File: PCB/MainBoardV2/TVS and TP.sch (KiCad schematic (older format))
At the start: 15 parts, among them U10 AOZ8318DI, U11 AOZ8318DI, U12 AOZ8318DI

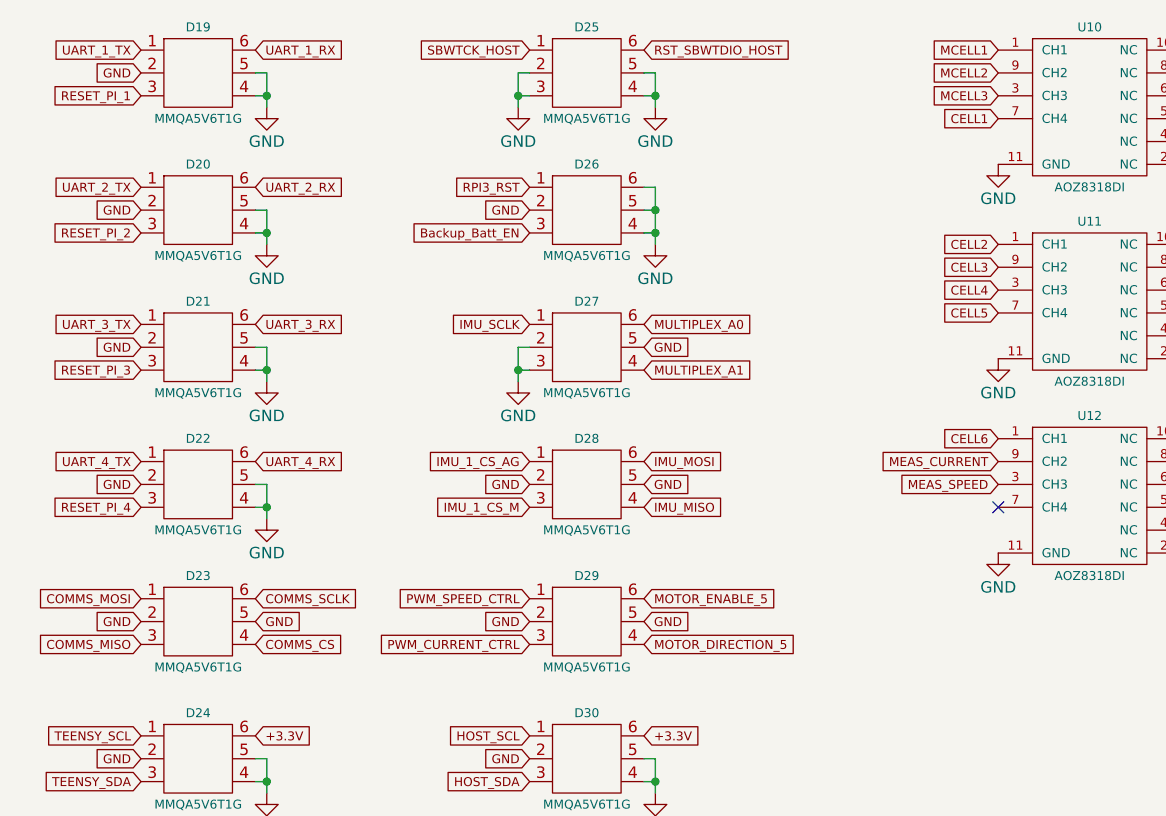
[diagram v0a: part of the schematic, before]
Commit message: Layout Done - Needs TPs Still
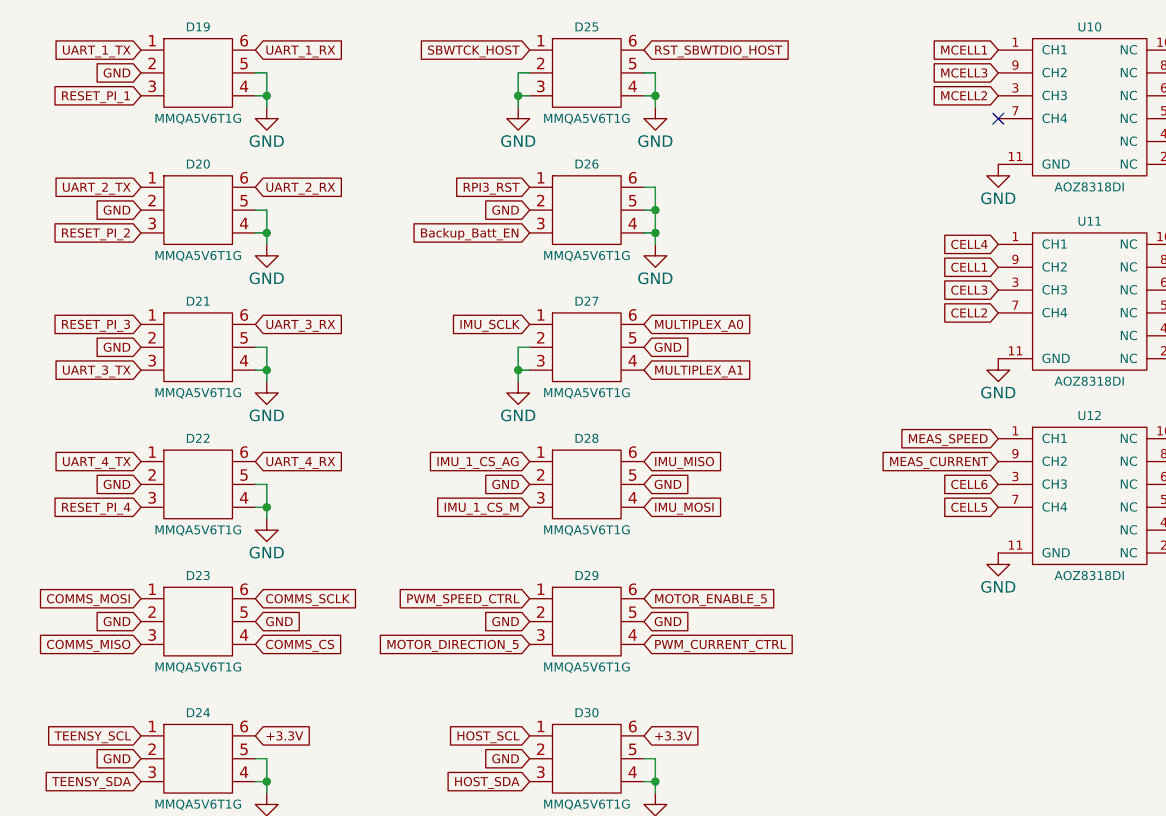
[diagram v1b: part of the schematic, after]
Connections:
- net CELL1: now also U11.9 (CH2); no longer U10.7 (CH4)
- net CELL2: now also U11.7 (CH4); no longer U11.1 (CH1)
- net CELL3: now also U11.3 (CH3); no longer U11.9 (CH2)
- net CELL4: now also U11.1 (CH1); no longer U11.3 (CH3)
- net CELL5: now also U12.7 (CH4); no longer U11.7 (CH4)
- net CELL6: now also U12.3 (CH3); no longer U12.1 (CH1)
- net IMU_MISO: now also D28.6; no longer D28.4
- net IMU_MOSI: now also D28.4; no longer D28.6
- net MCELL2: now also U10.3 (CH3); no longer U10.9 (CH2)
- net MCELL3: now also U10.9 (CH2); no longer U10.3 (CH3)
- net MEAS_SPEED: now also U12.1 (CH1); no longer U12.3 (CH3)
- net MOTOR_DIRECTION_5: now also D29.3; no longer D29.4
- net PWM_CURRENT_CTRL: now also D29.4; no longer D29.3
- net RESET_PI_3: now also D21.1; no longer D21.3
- net UART_3_TX: now also D21.3; no longer D21.1
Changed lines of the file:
@@
 RESET_PI_1
 $Comp
-L GND #PWR60
+L GND #PWR061
 U 1 1 5A7224CC
 P 1650 1350
-F 0 "#PWR60" H 1650 1100 50  0001 C CNN
+F 0 "#PWR061" H 1650 1100 50  0001 C CNN
 F 1 "GND" H 1650 1200 50  0000 C CNN
 F 2 "" H 1650 1350 50  0000 C CNN
@@
 RESET_PI_2
 $Comp
-L GND #PWR61
+L GND #PWR062
 U 1 1 5A722ECA
 P 1650 1950
-F 0 "#PWR61" H 1650 1700 50  0001 C CNN
+F 0 "#PWR062" H 1650 1700 50  0001 C CNN
 F 1 "GND" H 1650 1800 50  0000 C CNN
 F 2 "" H 1650 1950 50  0000 C CNN
@@
 	1    0    0    -1
 $EndComp
-Text GLabel 1100 2300 0    39   Input ~ 0
+Text GLabel 1100 2500 0    39   Input ~ 0
 UART_3_TX
 Text GLabel 1600 2300 2    39   Input ~ 0
 UART_3_RX
-Text GLabel 1100 2500 0    39   Input ~ 0
+Text GLabel 1100 2300 0    39   Input ~ 0
 RESET_PI_3
 $Comp
-L GND #PWR62
+L GND #PWR063
 U 1 1 5A722F46
 P 1650 2550
-F 0 "#PWR62" H 1650 2300 50  0001 C CNN
+F 0 "#PWR063" H 1650 2300 50  0001 C CNN
 F 1 "GND" H 1650 2400 50  0000 C CNN
 F 2 "" H 1650 2550 50  0000 C CNN
@@
 RESET_PI_4
 $Comp
-L GND #PWR63
+L GND #PWR064
 U 1 1 5A722F5A
 P 1650 3150
-F 0 "#PWR63" H 1650 2900 50  0001 C CNN
+F 0 "#PWR064" H 1650 2900 50  0001 C CNN
 F 1 "GND" H 1650 3000 50  0000 C CNN
 F 2 "" H 1650 3150 50  0000 C CNN
@@
 GND
 $Comp
-L GND #PWR64
+L GND #PWR065
 U 1 1 5A725481
 P 1650 4350
-F 0 "#PWR64" H 1650 4100 50  0001 C CNN
+F 0 "#PWR065" H 1650 4100 50  0001 C CNN
 F 1 "GND" H 1650 4200 50  0000 C CNN
 F 2 "" H 1650 4350 50  0000 C CNN
@@
 GND
 $Comp
-L GND #PWR69
+L GND #PWR066
 U 1 1 5A726700
 P 3350 4350
-F 0 "#PWR69" H 3350 4100 50  0001 C CNN
+F 0 "#PWR066" H 3350 4100 50  0001 C CNN
 F 1 "GND" H 3350 4200 50  0000 C CNN
 F 2 "" H 3350 4350 50  0000 C CNN
@@
 Text GLabel 3300 3500 2    39   Input ~ 0
 MOTOR_ENABLE_5
-Text GLabel 2800 3700 0    39   Input ~ 0
+Text GLabel 3300 3700 2    39   Input ~ 0
 PWM_CURRENT_CTRL
 Text GLabel 2800 3600 0    39   Input ~ 0
 GND
-Text GLabel 3300 3700 2    39   Input ~ 0
+Text GLabel 2800 3700 0    39   Input ~ 0
 MOTOR_DIRECTION_5
 Text GLabel 3300 3600 2    39   Input ~ 0
@@
 RST_SBWTDIO_HOST
 $Comp
-L GND #PWR67
+L GND #PWR067
 U 1 1 5A72776B
 P 3350 1350
-F 0 "#PWR67" H 3350 1100 50  0001 C CNN
+F 0 "#PWR067" H 3350 1100 50  0001 C CNN
 F 1 "GND" H 3350 1200 50  0000 C CNN
 F 2 "" H 3350 1350 50  0000 C CNN
@@
 Connection ~ 3350 1300
 $Comp
-L GND #PWR65
+L GND #PWR068
 U 1 1 5A72793A
 P 2750 1350
-F 0 "#PWR65" H 2750 1100 50  0001 C CNN
+F 0 "#PWR068" H 2750 1100 50  0001 C CNN
 F 1 "GND" H 2750 1200 50  0000 C CNN
 F 2 "" H 2750 1350 50  0000 C CNN
@@
 Text GLabel 2800 2900 0    39   Input ~ 0
 IMU_1_CS_AG
-Text GLabel 3300 2900 2    39   Input ~ 0
+Text GLabel 3300 3100 2    39   Input ~ 0
 IMU_MOSI
 Text GLabel 2800 3100 0    39   Input ~ 0
@@
 Text GLabel 2800 3000 0    39   Input ~ 0
 GND
-Text GLabel 3300 3100 2    39   Input ~ 0
+Text GLabel 3300 2900 2    39   Input ~ 0
 IMU_MISO
 Text GLabel 3300 3000 2    39   Input ~ 0
@@
 	1    0    0    -1
 $EndComp
-Text GLabel 2800 2300 0    39   Input ~ 0
-IMU_SCLK
 Text GLabel 3300 2300 2    39   Input ~ 0
 MULTIPLEX_A0
@@
 GND
 $Comp
-L GND #PWR66
+L GND #PWR069
 U 1 1 5A72903E
 P 2750 2550
-F 0 "#PWR66" H 2750 2300 50  0001 C CNN
+F 0 "#PWR069" H 2750 2300 50  0001 C CNN
 F 1 "GND" H 2750 2400 50  0000 C CNN
 F 2 "" H 2750 2550 50  0000 C CNN
@@
 Backup_Batt_EN
 $Comp
-L GND #PWR68
+L GND #PWR070
 U 1 1 5A72CB39
 P 3350 1950
-F 0 "#PWR68" H 3350 1700 50  0001 C CNN
+F 0 "#PWR070" H 3350 1700 50  0001 C CNN
 F 1 "GND" H 3350 1800 50  0000 C CNN
 F 2 "" H 3350 1950 50  0000 C CNN
@@
 $EndComp
 $Comp
-L GND #PWR70
+L GND #PWR071
 U 1 1 5A7569F3
 P 4850 1600
-F 0 "#PWR70" H 4850 1350 50  0001 C CNN
+F 0 "#PWR071" H 4850 1350 50  0001 C CNN
 F 1 "GND" H 4850 1450 50  0000 C CNN
 F 2 "" H 4850 1600 50  0000 C CNN
@@
 $EndComp
 $Comp
-L GND #PWR71
+L GND #PWR072
 U 1 1 5A756A23
 P 4850 2450
-F 0 "#PWR71" H 4850 2200 50  0001 C CNN
+F 0 "#PWR072" H 4850 2200 50  0001 C CNN
 F 1 "GND" H 4850 2300 50  0000 C CNN
 F 2 "" H 4850 2450 50  0000 C CNN
@@
 Text GLabel 4850 1100 0    39   Input ~ 0
 MCELL1
+Text GLabel 4850 1300 0    39   Input ~ 0
+MCELL2
 Text GLabel 4850 1200 0    39   Input ~ 0
-MCELL2
-Text GLabel 4850 1300 0    39   Input ~ 0
 MCELL3
-Text GLabel 4850 1400 0    39   Input ~ 0
+Text GLabel 4850 2050 0    39   Input ~ 0
 CELL1
+Text GLabel 4850 2250 0    39   Input ~ 0
+CELL2
+Text GLabel 4850 2150 0    39   Input ~ 0
+CELL3
 Text GLabel 4850 1950 0    39   Input ~ 0
-CELL2
-Text GLabel 4850 2050 0    39   Input ~ 0
-CELL3
-Text GLabel 4850 2150 0    39   Input ~ 0
 CELL4
-Text GLabel 4850 2250 0    39   Input ~ 0
+Text GLabel 4850 3100 0    39   Input ~ 0
 CELL5
 $Comp
@@
 $EndComp
 $Comp
-L GND #PWR72
+L GND #PWR073
 U 1 1 5A757EF3
 P 4850 3300
-F 0 "#PWR72" H 4850 3050 50  0001 C CNN
+F 0 "#PWR073" H 4850 3050 50  0001 C CNN
 F 1 "GND" H 4850 3150 50  0000 C CNN
 F 2 "" H 4850 3300 50  0000 C CNN
@@
 NoConn ~ 5650 3200
 NoConn ~ 5650 3300
-Text GLabel 4850 2800 0    39   Input ~ 0
+Text GLabel 4850 3000 0    39   Input ~ 0
 CELL6
 Text GLabel 4850 2900 0    39   Input ~ 0
 MEAS_CURRENT
-Text GLabel 4850 3000 0    39   Input ~ 0
+Text GLabel 4850 2800 0    39   Input ~ 0
 MEAS_SPEED
-NoConn ~ 4850 3100
 Wire Wire Line
 	3300 1700 3350 1700
 Connection ~ 3350 1800
+NoConn ~ 4850 1400
+Text GLabel 2800 2300 0    39   Input ~ 0
+IMU_SCLK
 $EndSCHEMATC

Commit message: Board Completed. Needs Review
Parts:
- added W1, W12, W13, W14, W17, W18, W2, W21, W23, W24, W27, W28, W29, W3, W32, W34, W35, W38, W39, W43, W45, W46, W49, W50, W54, W55, W56, W57, W6, W60, W61, W65, W7: TEST_1P, Connect:PINTST, symbol TEST_1P
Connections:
- net +3.3V: now also W29.1
- net COMMS_CS: now also W57.1
- net COMMS_MISO: now also W35.1
- net COMMS_MOSI: now also W24.1
- net COMMS_SCLK: now also W46.1
- net HOST_SCL: now also W3.1
- net HOST_SDA: now also W14.1
- net MOTOR_DIRECTION_5: now also W27.1
- net MOTOR_ENABLE_5: now also W38.1
- net MULTIPLEX_A0: now also W49.1
- net MULTIPLEX_A1: now also W60.1
- net RESET_PI_1: now also W21.1
- net RESET_PI_2: now also W32.1
- net RESET_PI_3: now also W43.1
- net RESET_PI_4: now also W54.1
- net RPI3_RST: now also W65.1
- net UART_1_RX: now also W12.1
- net UART_1_TX: now also W1.1
- net UART_2_RX: now also W34.1
- net UART_2_TX: now also W23.1
- net UART_3_RX: now also W56.1
- net UART_3_TX: now also W45.1
- net UART_4_RX: now also W13.1
- net UART_4_TX: now also W2.1
- new net +5V: W18.1
- new net +6.5V: W61.1
- new net Battery_Power: W50.1
- new net CUTDOWN_EN: W55.1
- new net From_Batt: W39.1
- new net From_LDO: W7.1
- new net MBATT: W6.1
- new net MBATT2: W17.1
- new net Main_Batt_EN: W28.1
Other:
- moved on the sheet: U10, U11, U12

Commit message: Added BOM, Couple Fixes, Couple Misc Documents
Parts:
- removed W49: TEST_1P, Connect:PINTST, symbol TEST_1P
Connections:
- net MULTIPLEX_A0: no longer names the net of D27.6
- net MULTIPLEX_A1: no longer names the net of D27.4
- net MULTIPLEX_A1: no longer W60.1
- new net MSP_GPIO_CB: W60.1
- no-connect marks 19 -> 21
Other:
- moved on the sheet: W55
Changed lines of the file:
@@
 	1    0    0    -1
 $EndComp
-Text GLabel 3300 2300 2    39   Input ~ 0
-MULTIPLEX_A0
-Text GLabel 3300 2500 2    39   Input ~ 0
-MULTIPLEX_A1
 Text GLabel 3300 2400 2    39   Input ~ 0
 GND
@@
 $EndComp
 $Comp
-L TEST_1P W49
-U 1 1 5A823E1D
-P 9000 2150
-F 0 "W49" H 9000 2420 50  0000 C CNN
-F 1 "TEST_1P" H 9000 2350 50  0000 C CNN
-F 2 "Connect:PINTST" H 9200 2150 50  0001 C CNN
-F 3 "" H 9200 2150 50  0000 C CNN
-	1    9000 2150
-	1    0    0    -1
-$EndComp
-$Comp
 L TEST_1P W60
 U 1 1 5A823E23
@@
 Text GLabel 8200 2150 0    39   Input ~ 0
 MOTOR_ENABLE_5
-Text GLabel 9000 2150 0    39   Input ~ 0
-MULTIPLEX_A0
 Text GLabel 9800 2150 0    39   Input ~ 0
-MULTIPLEX_A1
+MSP_GPIO_CB
 $Comp
 L TEST_1P W7
@@
 L TEST_1P W55
 U 1 1 5A844B00
-P 7400 3400
-F 0 "W55" H 7400 3670 50  0000 C CNN
-F 1 "TEST_1P" H 7400 3600 50  0000 C CNN
-F 2 "Connect:PINTST" H 7600 3400 50  0001 C CNN
-F 3 "" H 7600 3400 50  0000 C CNN
-	1    7400 3400
-	1    0    0    -1
-$EndComp
-Text GLabel 7400 3400 0    39   Input ~ 0
+P 9000 2150
+F 0 "W55" H 9000 2420 50  0000 C CNN
+F 1 "TEST_1P" H 9000 2350 50  0000 C CNN
+F 2 "Connect:PINTST" H 9200 2150 50  0001 C CNN
+F 3 "" H 9200 2150 50  0000 C CNN
+	1    9000 2150
+	1    0    0    -1
+$EndComp
+Text GLabel 9000 2150 0    39   Input ~ 0
 CUTDOWN_EN
 $Comp
@@
 Text GLabel 7400 2150 0    39   Input ~ 0
 MOTOR_DIRECTION_5
+NoConn ~ 3300 2300
+NoConn ~ 3300 2500
 $EndSCHEMATC
